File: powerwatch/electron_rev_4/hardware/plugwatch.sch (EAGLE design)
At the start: 124 parts, among them J1 DM3AT-SF-PEJM5, Q1 SI223DDS, Q3 MOSFET-NCHANNELSMD, Q4 NX3008PBK, U1 BGA725L6-ALT, U10 SIP32510, U12 SIP32510, U13 AB1815-T3, U16 MAX6746, U2 SAFFB1G56KB0F0A, U3 IRM-03-5V, U4 MAX-M8, U5 MAX9910, U6 LIS2DW12, U8 MAX9910, U9 SIP32510, X1 ABS07-32.768KHZ-7-T

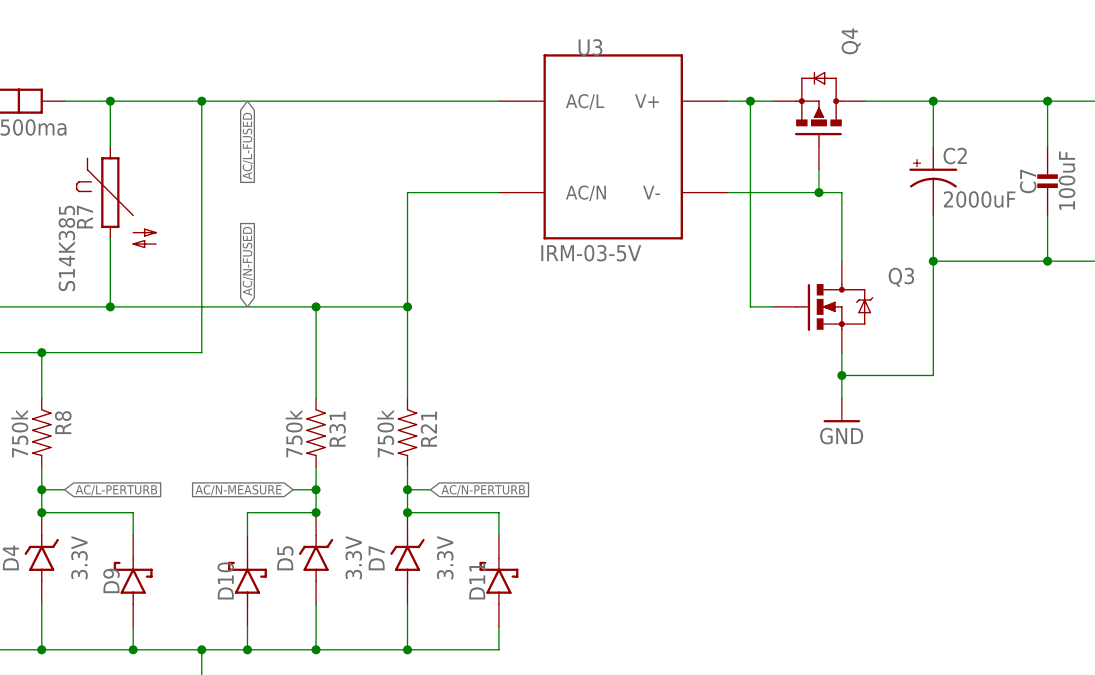
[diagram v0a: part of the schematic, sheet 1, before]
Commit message: remove mosfets - I don't think they are necessary
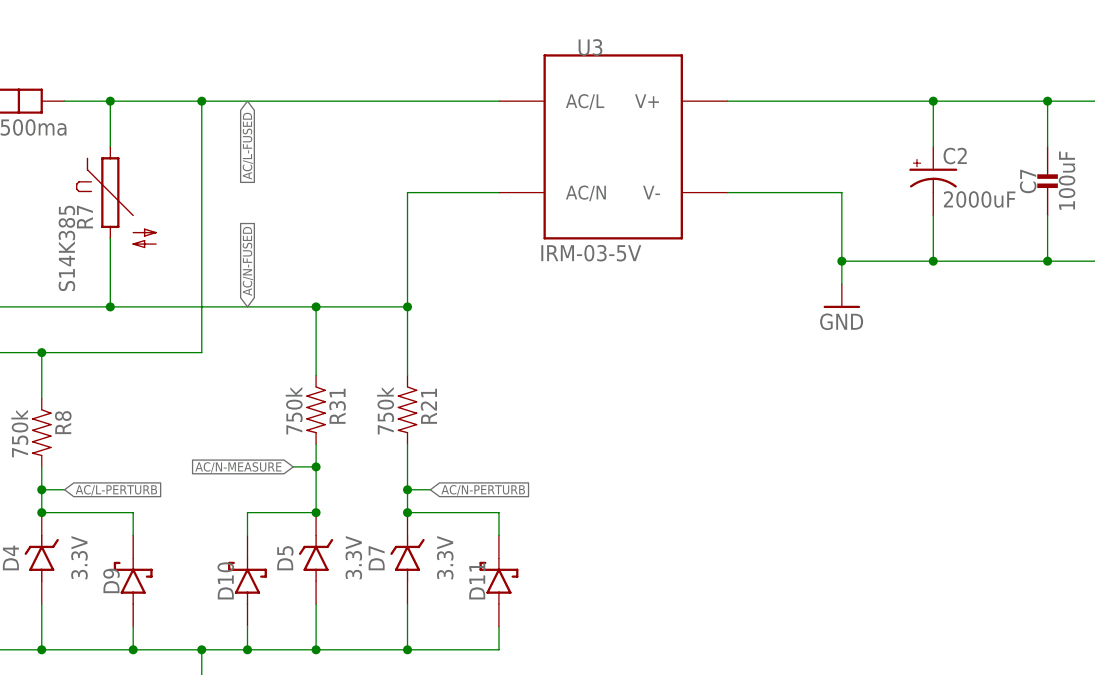
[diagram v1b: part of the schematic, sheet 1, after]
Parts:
- removed Q3: MOSFET-NCHANNELSMD, fets:MOSFET-NCHANNELSMD
- removed Q4: NX3008PBK, fets:NX3008PBK
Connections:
- removed net N$32: Q3.G, Q4.S, U3.V+
- removed net N$8: Q3.D, Q4.G, U3.V-
- net 5V: now also U3.V+; no longer Q4.D
- net GND: now also U3.V-; no longer Q3.S
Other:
- note removed: "This mosfet should turn on when power is supplied by the circuit - otherwise we float GND for capacitance measurement."
- moved on the sheet: R21, R31
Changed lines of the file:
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@@
 <drawing>
 <settings>
-<setting alwaysvectorfont="yes"/>
+<setting alwaysvectorfont="no"/>
 <setting verticaltext="up"/>
 </settings>
@@
 <part name="TP16" library="headers" deviceset="TEST_POINT_0.040IN" device=""/>
 <part name="TP17" library="headers" deviceset="TEST_POINT_0.040IN" device=""/>
-<part name="Q3" library="fets" deviceset="MOSFET-NCHANNEL" device="SMD"/>
-<part name="Q4" library="fets" deviceset="NX3008PBK" device=""/>
 </parts>
 <sheets>
@@
 <plain>
 <text x="167.64" y="177.8" size="1.016" layer="98" align="bottom-center">The peak power is 2A * 600uS = ~4.5mJ. We are adding 8mJ of energy buffer to be safe. 8mJ of energy with a 5V to 4V swing is about 2mF</text>
-<text x="157.48" y="132.08" size="1.016" layer="98" align="bottom-center">This mosfet should turn on when
- power is supplied by the circuit
- - otherwise we float GND for
- capacitance measurement.</text>
 <text x="53.34" y="177.8" size="1.016" layer="98" align="bottom-center">This will protect the sampling circuit against surges</text>
 <text x="30.48" y="86.36" size="1.778" layer="97">Output voltage:</text>
@@
 <text x="55.88" y="33.02" size="1.016" layer="98" align="bottom-center">This circuit handles up to 340V with a 3.3V reference.</text>
 <text x="137.16" y="33.02" size="1.016" layer="98" align="bottom-center">This circuit handles up to 340V with a 3.3V reference.</text>
-<text x="66.04" y="137.16" size="1.016" layer="98" align="bottom-center">We use a seperate AC Measure pin so that we can more directly sense the perturbation by the digital output.
+<text x="66.04" y="139.7" size="1.016" layer="98" align="bottom-center">We use a seperate AC Measure pin so that we can more directly sense the perturbation by the digital output.
 The full-scale voltage sensing circuit (below) could also be used, but would only sense &lt;1% of its dynamic range.</text>
 </plain>
@@
 <instance part="AC/L" gate="G$1" x="35.56" y="170.18"/>
 <instance part="AC/N" gate="G$1" x="35.56" y="147.32"/>
-<instance part="SUPPLY1" gate="1" x="142.24" y="134.62"/>
+<instance part="SUPPLY1" gate="1" x="142.24" y="147.32"/>
 <instance part="C2" gate="G$1" x="152.4" y="162.56"/>
 <instance part="C7" gate="G$1" x="165.1" y="162.56"/>
@@
 </instance>
 <instance part="SUPPLY2" gate="1" x="71.12" y="99.06"/>
-<instance part="R21" gate="G$1" x="93.98" y="132.08" rot="R270">
-<attribute name="DIGIKEY" x="93.98" y="132.08" size="1.27" layer="96" rot="R270" display="off"/>
+<instance part="R21" gate="G$1" x="93.98" y="134.62" rot="R270">
+<attribute name="DIGIKEY" x="93.98" y="134.62" size="1.27" layer="96" rot="R270" display="off"/>
 </instance>
 <instance part="U5" gate="G$1" x="63.5" y="60.96"/>
@@
 <attribute name="MPN" x="43.18" y="119.38" size="1.016" layer="96" rot="R90" align="bottom-center" display="off"/>
 </instance>
-<instance part="R31" gate="G$1" x="83.82" y="132.08" rot="R270">
-<attribute name="DIGIKEY" x="83.82" y="132.08" size="1.27" layer="96" rot="R270" display="off"/>
+<instance part="R31" gate="G$1" x="83.82" y="134.62" rot="R270">
+<attribute name="DIGIKEY" x="83.82" y="134.62" size="1.27" layer="96" rot="R270" display="off"/>
 </instance>
 <instance part="D8" gate="G$1" x="35.56" y="116.84" rot="R90">
@@
 <attribute name="MANUFACTURER" x="93.98" y="119.38" size="1.016" layer="96" rot="R90" align="bottom-center" display="off"/>
 <attribute name="MPN" x="93.98" y="119.38" size="1.016" layer="96" rot="R90" align="bottom-center" display="off"/>
-</instance>
-<instance part="Q3" gate="G$1" x="142.24" y="147.32" smashed="yes">
-<attribute name="NAME" x="147.32" y="149.86" size="1.778" layer="95"/>
-</instance>
-<instance part="Q4" gate="G$1" x="139.7" y="170.18" smashed="yes" rot="MR90">
-<attribute name="NAME" x="142.24" y="175.26" size="1.778" layer="95" rot="MR90"/>
 </instance>
 </instances>
@@
 <junction x="60.96" y="147.32"/>
 <pinref part="R21" gate="G$1" pin="1"/>
-<wire x1="93.98" y1="137.16" x2="93.98" y2="147.32" width="0.1524" layer="91"/>
+<wire x1="93.98" y1="139.7" x2="93.98" y2="147.32" width="0.1524" layer="91"/>
 <junction x="93.98" y="147.32"/>
 <label x="76.2" y="147.32" size="1.016" layer="95" rot="R90" xref="yes"/>
 <pinref part="R31" gate="G$1" pin="1"/>
-<wire x1="83.82" y1="137.16" x2="83.82" y2="147.32" width="0.1524" layer="91"/>
+<wire x1="83.82" y1="139.7" x2="83.82" y2="147.32" width="0.1524" layer="91"/>
 <junction x="83.82" y="147.32"/>
 </segment>
@@
 <pinref part="C7" gate="G$1" pin="1"/>
 <pinref part="C17" gate="G$1" pin="1"/>
-<pinref part="Q4" gate="G$1" pin="D"/>
-<wire x1="144.78" y1="170.18" x2="152.4" y2="170.18" width="0.1524" layer="91"/>
 <junction x="152.4" y="170.18"/>
+<pinref part="U3" gate="G$1" pin="V+"/>
+<wire x1="129.54" y1="170.18" x2="152.4" y2="170.18" width="0.1524" layer="91"/>
 </segment>
 </net>
 <net name="GND" class="0">
-<segment>
-<pinref part="SUPPLY1" gate="1" pin="GND"/>
-<wire x1="142.24" y1="137.16" x2="142.24" y2="139.7" width="0.1524" layer="91"/>
-<wire x1="152.4" y1="157.48" x2="152.4" y2="152.4" width="0.1524" layer="91"/>
-<wire x1="165.1" y1="157.48" x2="165.1" y2="152.4" width="0.1524" layer="91"/>
-<wire x1="165.1" y1="152.4" x2="152.4" y2="152.4" width="0.1524" layer="91"/>
-<wire x1="177.8" y1="157.48" x2="177.8" y2="152.4" width="0.1524" layer="91"/>
-<wire x1="177.8" y1="152.4" x2="165.1" y2="152.4" width="0.1524" layer="91"/>
-<junction x="165.1" y="152.4"/>
-<pinref part="C2" gate="G$1" pin="-"/>
-<pinref part="C7" gate="G$1" pin="2"/>
-<pinref part="C17" gate="G$1" pin="2"/>
-<wire x1="152.4" y1="152.4" x2="152.4" y2="139.7" width="0.1524" layer="91"/>
-<junction x="152.4" y="152.4"/>
-<wire x1="152.4" y1="139.7" x2="142.24" y2="139.7" width="0.1524" layer="91"/>
-<junction x="142.24" y="139.7"/>
-<pinref part="Q3" gate="G$1" pin="S"/>
-<wire x1="142.24" y1="139.7" x2="142.24" y2="142.24" width="0.1524" layer="91"/>
-</segment>
 <segment>
 <pinref part="SUPPLY2" gate="1" pin="GND"/>
@@
 <pinref part="SUPPLY10" gate="1" pin="GND"/>
 </segment>
-</net>
-<net name="N$32" class="0">
-<segment>
-<pinref part="Q3" gate="G$1" pin="G"/>
-<wire x1="134.62" y1="147.32" x2="132.08" y2="147.32" width="0.1524" layer="91"/>
-<pinref part="U3" gate="G$1" pin="V+"/>
-<wire x1="129.54" y1="170.18" x2="132.08" y2="170.18" width="0.1524" layer="91"/>
-<wire x1="132.08" y1="147.32" x2="132.08" y2="170.18" width="0.1524" layer="91"/>
-<pinref part="Q4" gate="G$1" pin="S"/>
-<wire x1="132.08" y1="170.18" x2="134.62" y2="170.18" width="0.1524" layer="91"/>
-<junction x="132.08" y="170.18"/>
+<segment>
+<wire x1="152.4" y1="157.48" x2="152.4" y2="152.4" width="0.1524" layer="91"/>
+<wire x1="165.1" y1="157.48" x2="165.1" y2="152.4" width="0.1524" layer="91"/>
+<wire x1="165.1" y1="152.4" x2="152.4" y2="152.4" width="0.1524" layer="91"/>
+<wire x1="177.8" y1="157.48" x2="177.8" y2="152.4" width="0.1524" layer="91"/>
+<wire x1="177.8" y1="152.4" x2="165.1" y2="152.4" width="0.1524" layer="91"/>
+<junction x="165.1" y="152.4"/>
+<pinref part="C2" gate="G$1" pin="-"/>
+<pinref part="C7" gate="G$1" pin="2"/>
+<pinref part="C17" gate="G$1" pin="2"/>
+<junction x="152.4" y="152.4"/>
+<pinref part="U3" gate="G$1" pin="V-"/>
+<wire x1="129.54" y1="160.02" x2="142.24" y2="160.02" width="0.1524" layer="91"/>
+<wire x1="142.24" y1="152.4" x2="142.24" y2="160.02" width="0.1524" layer="91"/>
+<wire x1="142.24" y1="152.4" x2="152.4" y2="152.4" width="0.1524" layer="91"/>
+<pinref part="SUPPLY1" gate="1" pin="GND"/>
+<wire x1="142.24" y1="149.86" x2="142.24" y2="152.4" width="0.1524" layer="91"/>
+<junction x="142.24" y="152.4"/>
 </segment>
 </net>
@@
 <pinref part="R21" gate="G$1" pin="2"/>
 <wire x1="93.98" y1="124.46" x2="93.98" y2="127" width="0.1524" layer="91"/>
-<wire x1="93.98" y1="127" x2="93.98" y2="129.54" width="0.1524" layer="91"/>
+<wire x1="93.98" y1="127" x2="93.98" y2="132.08" width="0.1524" layer="91"/>
 <wire x1="93.98" y1="127" x2="96.52" y2="127" width="0.1524" layer="91"/>
 <junction x="93.98" y="127"/>
@@
 <segment>
 <pinref part="R31" gate="G$1" pin="2"/>
-<wire x1="83.82" y1="129.54" x2="83.82" y2="127" width="0.1524" layer="91"/>
-<wire x1="83.82" y1="127" x2="83.82" y2="124.46" width="0.1524" layer="91"/>
-<wire x1="83.82" y1="127" x2="81.28" y2="127" width="0.1524" layer="91"/>
-<junction x="83.82" y="127"/>
-<label x="81.28" y="127" size="1.016" layer="95" rot="R180" xref="yes"/>
+<wire x1="83.82" y1="132.08" x2="83.82" y2="129.54" width="0.1524" layer="91"/>
+<wire x1="83.82" y1="129.54" x2="83.82" y2="124.46" width="0.1524" layer="91"/>
+<wire x1="83.82" y1="129.54" x2="81.28" y2="129.54" width="0.1524" layer="91"/>
+<junction x="83.82" y="129.54"/>
+<label x="81.28" y="129.54" size="1.016" layer="95" rot="R180" xref="yes"/>
 <wire x1="76.2" y1="121.92" x2="76.2" y2="124.46" width="0.1524" layer="91"/>
 <wire x1="76.2" y1="124.46" x2="83.82" y2="124.46" width="0.1524" layer="91"/>
@@
 </segment>
 </net>
-<net name="N$8" class="0">
-<segment>
-<pinref part="U3" gate="G$1" pin="V-"/>
-<wire x1="129.54" y1="160.02" x2="139.7" y2="160.02" width="0.1524" layer="91"/>
-<pinref part="Q3" gate="G$1" pin="D"/>
-<wire x1="139.7" y1="160.02" x2="142.24" y2="160.02" width="0.1524" layer="91"/>
-<wire x1="142.24" y1="152.4" x2="142.24" y2="160.02" width="0.1524" layer="91"/>
-<pinref part="Q4" gate="G$1" pin="G"/>
-<wire x1="139.7" y1="162.56" x2="139.7" y2="160.02" width="0.1524" layer="91"/>
-<junction x="139.7" y="160.02"/>
-</segment>
-</net>
